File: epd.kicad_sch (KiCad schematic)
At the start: 19 parts, among them J401 FH12A-24S-0.5SH(55), Q401 Q_NMOS_GSD

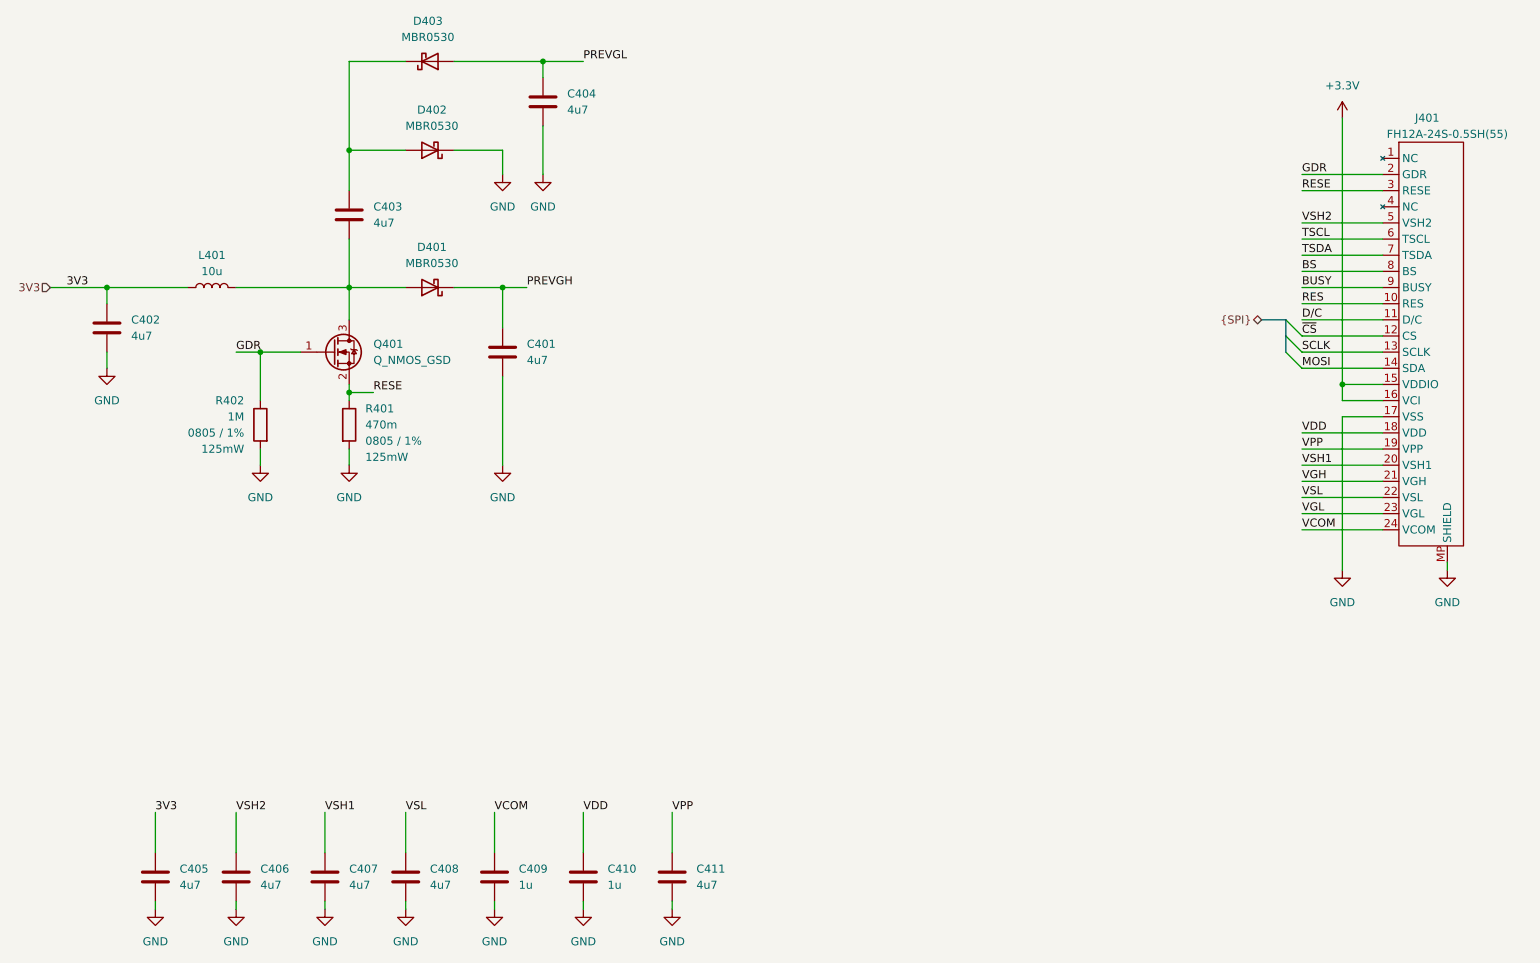
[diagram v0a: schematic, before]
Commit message: Switch to 16 pin USB-C
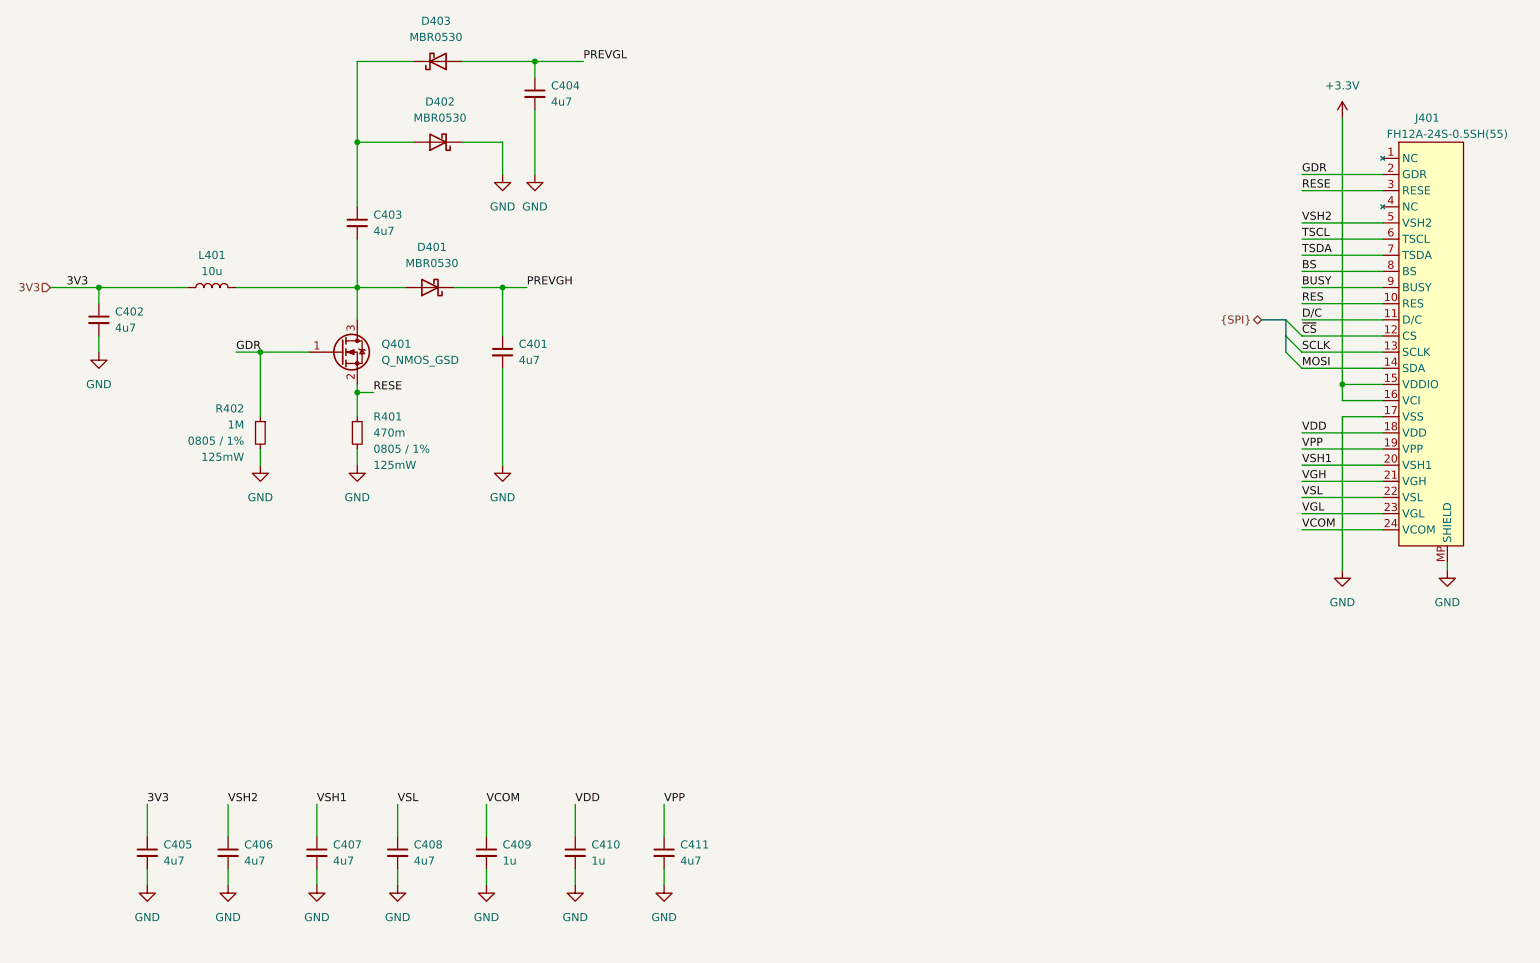
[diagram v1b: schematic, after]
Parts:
- C401, C402, C403, C404, C405, C406, C407, C408, C409, C410, C411: symbol Device:C -> Device:C_Small
- R401, R402: symbol Device:R -> Device:R_Small
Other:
- moved on the sheet: C402, C403, C404, C405, C406, C407, C408, C409, C410, C411, D402, D403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

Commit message: Correct SPI pinout
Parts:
- C401, C402, C403, C404, C405, C406, C407, C408, C409, C410, C411: Dielectric (none) -> X7R
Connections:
- net +3.3V is gone; now on net 3V3: J401.15 (VDDIO), J401.16 (VCI)
- net BS is gone; now on net GND: J401.8 (BS)
- net VGH is gone; now on net PREVGH: J401.21 (VGH)
- net VGL is gone; now on net PREVGL: J401.23 (VGL)
- net BUSY renamed EPD_BUSY
- net D/C renamed EPD_D/C
- net MOSI renamed SPI.MOSI
- net RES renamed EPD_RST
- net SCLK renamed SPI.SCLK
- net TSCL: no longer names the net of J401.6 (TSCL)
- net TSDA: no longer names the net of J401.7 (TSDA)
- net ~{CS} renamed SPI.~{CS}
- no-connect marks 0 -> 2

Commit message: Finish everything
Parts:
- J401: symbol busbuddy:FPC24 -> busbuddy:FPC24_Inverted
- Q401: LCSC Part Number (none) -> C469327
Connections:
- net 3V3: now also J401.10 (VDDIO), J401.9 (VCI); no longer J401.15 (VDDIO), J401.16 (VCI)
- net EPD_BUSY: now also J401.16 (BUSY); no longer J401.9 (BUSY)
- net EPD_D/C: now also J401.14 (D/C); no longer J401.11 (D/C)
- net EPD_RST: now also J401.15 (RES); no longer J401.10 (RES)
- net GDR: now also J401.23 (GDR); no longer J401.2 (GDR)
- net PREVGH: now also J401.4 (VGH); no longer J401.21 (VGH)
- net PREVGL: now also J401.2 (VGL); no longer J401.23 (VGL)
- net RESE: now also J401.22 (RESE); no longer J401.3 (RESE)
- net SPI.MOSI: now also J401.11 (SDA); no longer J401.14 (SDA)
- net SPI.SCLK: now also J401.12 (SCLK); no longer J401.13 (SCLK)
- net SPI.~{CS}: now also J401.13 (CS); no longer J401.12 (CS)
- net VCOM: now also J401.1 (VCOM); no longer J401.24 (VCOM)
- net VDD: now also J401.7 (VDD); no longer J401.18 (VDD)
- net VPP: now also J401.6 (VPP); no longer J401.19 (VPP)
- net VSH1: now also J401.5 (VSH1); no longer J401.20 (VSH1)
- net VSH2: now also J401.20 (VSH2); no longer J401.5 (VSH2)
- net VSL: now also J401.3 (VSL); no longer J401.22 (VSL)
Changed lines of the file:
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@@
 			)
 		)
-		(property "LCSC Part Number" ""
+		(property "LCSC Part Number" "C469327"
 			(at 83.82 86.36 0)
 			(effects
@@
 	)
 	(symbol
-		(lib_id "busbuddy:FPC24")
+		(lib_id "busbuddy:FPC24_Inverted")
 		(at 255.27 85.09 0)
 		(unit 1)

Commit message: Rename project
Damn squatters
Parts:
- J401: symbol busbuddy:FPC24_Inverted -> youdbetterrun:FPC24_Inverted
- L401: footprint busbuddy:L_4x4x2.6 -> youdbetterrun:L_4x4x2.6
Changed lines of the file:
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@@
 		)
 		(instances
-			(project "busbuddy"
+			(project "youdbetterrun"
 				(path "/50da2b4e-34b1-4787-8ee6-5d7d17f804f4/d598949e-74c6-4803-8db9-612ef03f3111"
 					(reference "C401")
@@
 		)
 		(instances
-			(project "busbuddy"
+			(project "youdbetterrun"
 				(path "/50da2b4e-34b1-4787-8ee6-5d7d17f804f4/d598949e-74c6-4803-8db9-612ef03f3111"
 					(reference "#PWR0411")
@@
 		)
 		(instances
-			(project "busbuddy"
+			(project "youdbetterrun"
 				(path "/50da2b4e-34b1-4787-8ee6-5d7d17f804f4/d598949e-74c6-4803-8db9-612ef03f3111"
 					(reference "#PWR0403")
@@
 		)
 		(instances
-			(project "busbuddy"
+			(project "youdbetterrun"
 				(path "/50da2b4e-34b1-4787-8ee6-5d7d17f804f4/d598949e-74c6-4803-8db9-612ef03f3111"
 					(reference "#FLG04")
@@
 		)
 		(instances
-			(project "busbuddy"
+			(project "youdbetterrun"
 				(path "/50da2b4e-34b1-4787-8ee6-5d7d17f804f4/d598949e-74c6-4803-8db9-612ef03f3111"
 					(reference "C409")
@@
 		)
 		(instances
-			(project "busbuddy"
+			(project "youdbetterrun"
 				(path "/50da2b4e-34b1-4787-8ee6-5d7d17f804f4/d598949e-74c6-4803-8db9-612ef03f3111"
 					(reference "C402")
@@
 		)
 		(instances
-			(project "busbuddy"
+			(project "youdbetterrun"
 				(path "/50da2b4e-34b1-4787-8ee6-5d7d17f804f4/d598949e-74c6-4803-8db9-612ef03f3111"
 					(reference "#PWR0415")
@@
 		)
 		(instances
-			(project "busbuddy"
+			(project "youdbetterrun"
 				(path "/50da2b4e-34b1-4787-8ee6-5d7d17f804f4/d598949e-74c6-4803-8db9-612ef03f3111"
 					(reference "#PWR0412")
@@
 			)
 		)
-		(property "Footprint" "busbuddy:L_4x4x2.6"
+		(property "Footprint" "youdbetterrun:L_4x4x2.6"
 			(at 63.5 76.2 0)
 			(effects
@@
 		)
 		(instances
-			(project "busbuddy"
+			(project "youdbetterrun"
 				(path "/50da2b4e-34b1-4787-8ee6-5d7d17f804f4/d598949e-74c6-4803-8db9-612ef03f3111"
 					(reference "L401")
@@
 		)
 		(instances
-			(project "busbuddy"
+			(project "youdbetterrun"
 				(path "/50da2b4e-34b1-4787-8ee6-5d7d17f804f4/d598949e-74c6-4803-8db9-612ef03f3111"
 					(reference "D402")
@@
 		)
 		(instances
-			(project "busbuddy"
+			(project "youdbetterrun"
 				(path "/50da2b4e-34b1-4787-8ee6-5d7d17f804f4/d598949e-74c6-4803-8db9-612ef03f3111"
 					(reference "C408")
@@
 		)
 		(instances
-			(project "busbuddy"
+			(project "youdbetterrun"
 				(path "/50da2b4e-34b1-4787-8ee6-5d7d17f804f4/d598949e-74c6-4803-8db9-612ef03f3111"
 					(reference "D401")
@@
 		)
 		(instances
-			(project "busbuddy"
+			(project "youdbetterrun"
 				(path "/50da2b4e-34b1-4787-8ee6-5d7d17f804f4/d598949e-74c6-4803-8db9-612ef03f3111"
 					(reference "#PWR0409")
@@
 		)
 		(instances
-			(project "busbuddy"
+			(project "youdbetterrun"
 				(path "/50da2b4e-34b1-4787-8ee6-5d7d17f804f4/d598949e-74c6-4803-8db9-612ef03f3111"
 					(reference "#PWR0406")
@@
 		)
 		(instances
-			(project "busbuddy"
+			(project "youdbetterrun"
 				(path "/50da2b4e-34b1-4787-8ee6-5d7d17f804f4/d598949e-74c6-4803-8db9-612ef03f3111"
 					(reference "#PWR0407")
@@
 		)
 		(instances
-			(project "busbuddy"
+			(project "youdbetterrun"
 				(path "/50da2b4e-34b1-4787-8ee6-5d7d17f804f4/d598949e-74c6-4803-8db9-612ef03f3111"
 					(reference "#PWR0405")
@@
 		)
 		(instances
-			(project "busbuddy"
+			(project "youdbetterrun"
 				(path "/50da2b4e-34b1-4787-8ee6-5d7d17f804f4/d598949e-74c6-4803-8db9-612ef03f3111"
 					(reference "R401")
@@
 		)
 		(instances
-			(project "busbuddy"
+			(project "youdbetterrun"
 				(path "/50da2b4e-34b1-4787-8ee6-5d7d17f804f4/d598949e-74c6-4803-8db9-612ef03f3111"
 					(reference "C405")
@@
 		)
 		(instances
-			(project "busbuddy"
+			(project "youdbetterrun"
 				(path "/50da2b4e-34b1-4787-8ee6-5d7d17f804f4/d598949e-74c6-4803-8db9-612ef03f3111"
 					(reference "#PWR0410")
@@
 		)
 		(instances
-			(project "busbuddy"
+			(project "youdbetterrun"
 				(path "/50da2b4e-34b1-4787-8ee6-5d7d17f804f4/d598949e-74c6-4803-8db9-612ef03f3111"
 					(reference "Q401")
@@
 		)
 		(instances
-			(project "busbuddy"
+			(project "youdbetterrun"
 				(path "/50da2b4e-34b1-4787-8ee6-5d7d17f804f4/d598949e-74c6-4803-8db9-612ef03f3111"
 					(reference "C404")
@@
 	)
 	(symbol
-		(lib_id "busbuddy:FPC24_Inverted")
+		(lib_id "youdbetterrun:FPC24_Inverted")
 		(at 255.27 85.09 0)
 		(unit 1)
@@
 		)
 		(instances
-			(project "busbuddy"
+			(project "youdbetterrun"
 				(path "/50da2b4e-34b1-4787-8ee6-5d7d17f804f4/d598949e-74c6-4803-8db9-612ef03f3111"
 					(reference "J401")
@@
 		)
 		(instances
-			(project "busbuddy"
+			(project "youdbetterrun"
 				(path "/50da2b4e-34b1-4787-8ee6-5d7d17f804f4/d598949e-74c6-4803-8db9-612ef03f3111"
 					(reference "#PWR0402")
@@
 		)
 		(instances
-			(project "busbuddy"
+			(project "youdbetterrun"
 				(path "/50da2b4e-34b1-4787-8ee6-5d7d17f804f4/d598949e-74c6-4803-8db9-612ef03f3111"
 					(reference "C411")
@@
 		)
 		(instances
-			(project "busbuddy"
+			(project "youdbetterrun"
 				(path "/50da2b4e-34b1-4787-8ee6-5d7d17f804f4/d598949e-74c6-4803-8db9-612ef03f3111"
 					(reference "#FLG05")
@@
 		)
 		(instances
-			(project "busbuddy"
+			(project "youdbetterrun"
 				(path "/50da2b4e-34b1-4787-8ee6-5d7d17f804f4/d598949e-74c6-4803-8db9-612ef03f3111"
 					(reference "#PWR0408")
@@
 		)
 		(instances
-			(project "busbuddy"
+			(project "youdbetterrun"
 				(path "/50da2b4e-34b1-4787-8ee6-5d7d17f804f4/d598949e-74c6-4803-8db9-612ef03f3111"
 					(reference "#PWR0404")
@@
 		)
 		(instances
-			(project "busbuddy"
+			(project "youdbetterrun"
 				(path "/50da2b4e-34b1-4787-8ee6-5d7d17f804f4/d598949e-74c6-4803-8db9-612ef03f3111"
 					(reference "#PWR0413")
@@
 		)
 		(instances
-			(project "busbuddy"
+			(project "youdbetterrun"
 				(path "/50da2b4e-34b1-4787-8ee6-5d7d17f804f4/d598949e-74c6-4803-8db9-612ef03f3111"
 					(reference "R402")
@@
 		)
 		(instances
-			(project "busbuddy"
+			(project "youdbetterrun"
 				(path "/50da2b4e-34b1-4787-8ee6-5d7d17f804f4/d598949e-74c6-4803-8db9-612ef03f3111"
 					(reference "#PWR0416")
@@
 		)
 		(instances
-			(project "busbuddy"
+			(project "youdbetterrun"
 				(path "/50da2b4e-34b1-4787-8ee6-5d7d17f804f4/d598949e-74c6-4803-8db9-612ef03f3111"
 					(reference "D403")
@@
 		)
 		(instances
-			(project "busbuddy"
+			(project "youdbetterrun"
 				(path "/50da2b4e-34b1-4787-8ee6-5d7d17f804f4/d598949e-74c6-4803-8db9-612ef03f3111"
 					(reference "C403")
@@
 		)
 		(instances
-			(project "busbuddy"
+			(project "youdbetterrun"
 				(path "/50da2b4e-34b1-4787-8ee6-5d7d17f804f4/d598949e-74c6-4803-8db9-612ef03f3111"
 					(reference "C406")
@@
 		)
 		(instances
-			(project "busbuddy"
+			(project "youdbetterrun"
 				(path "/50da2b4e-34b1-4787-8ee6-5d7d17f804f4/d598949e-74c6-4803-8db9-612ef03f3111"
 					(reference "C410")
@@
 		)
 		(instances
-			(project "busbuddy"
+			(project "youdbetterrun"
 				(path "/50da2b4e-34b1-4787-8ee6-5d7d17f804f4/d598949e-74c6-4803-8db9-612ef03f3111"
 					(reference "C407")
@@
 		)
 		(instances
-			(project "busbuddy"
+			(project "youdbetterrun"
 				(path "/50da2b4e-34b1-4787-8ee6-5d7d17f804f4/d598949e-74c6-4803-8db9-612ef03f3111"
 					(reference "#PWR0414")
